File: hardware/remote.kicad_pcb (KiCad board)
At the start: 2 copper layers, 40 x 25 mm, 18 parts, among them P1 CON-SENSOR, U1 M24C64, U2 RFM69HW, U3 DRILL, U4 DRILL, U5 DRILL, U6 DRILL

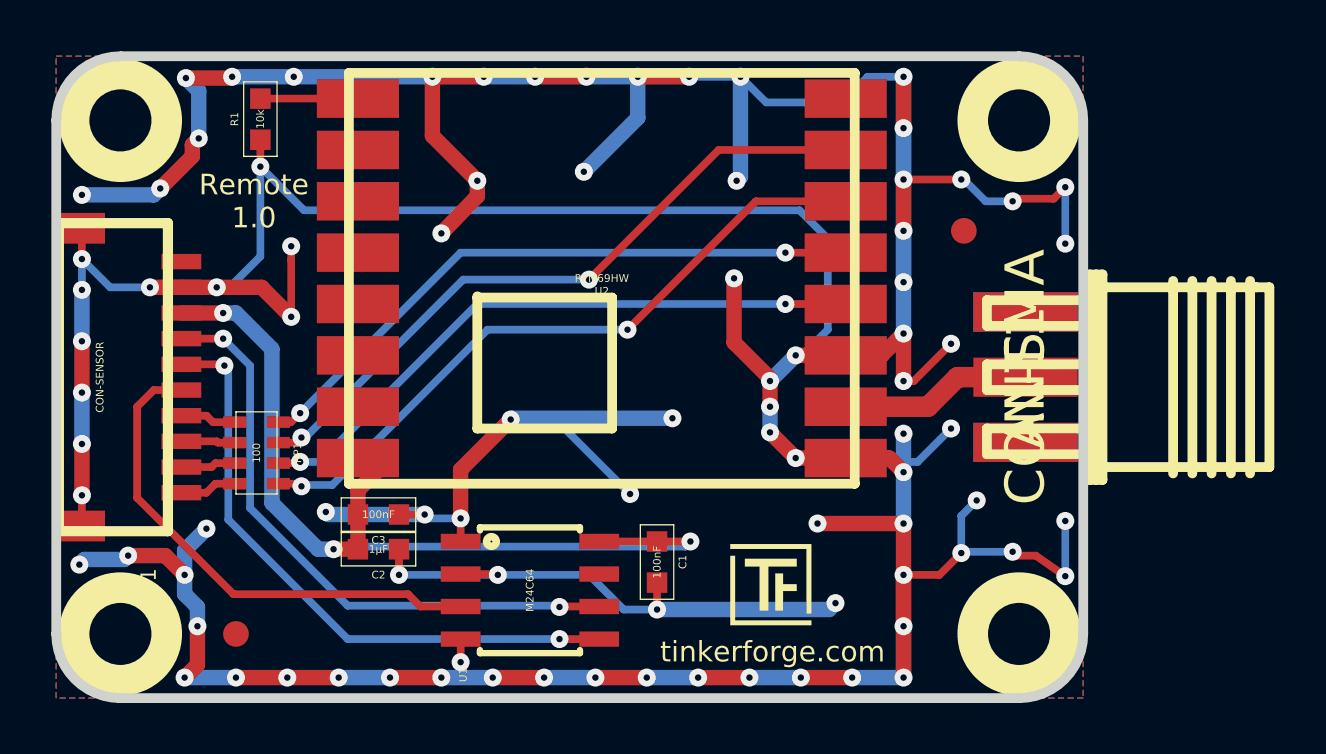
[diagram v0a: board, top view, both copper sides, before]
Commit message: update silkscreen outlines
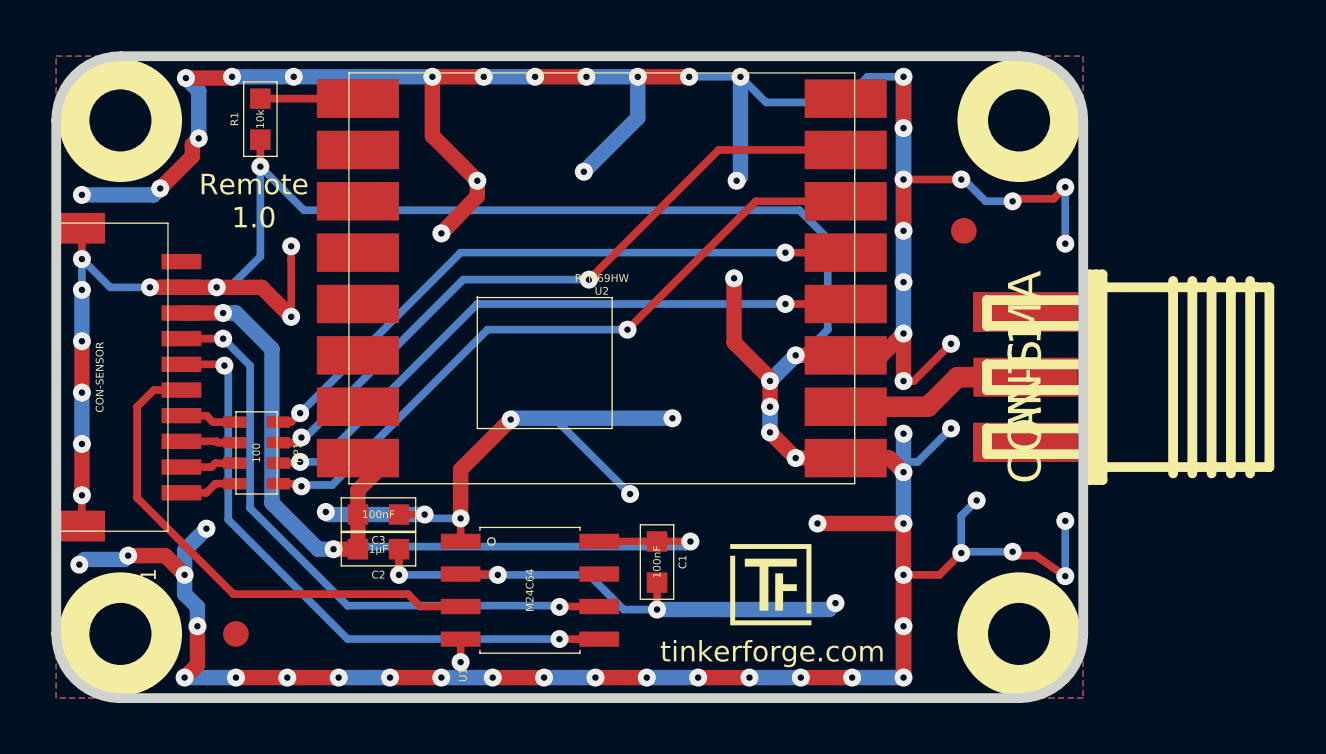
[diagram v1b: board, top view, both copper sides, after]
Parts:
- P1: footprint CON-SENSOR -> tinkerforge:CON-SENSOR
- U1: footprint SOIC8 -> tinkerforge:SOIC8
- U2: footprint RFM69HW -> tinkerforge:RFM69HW
